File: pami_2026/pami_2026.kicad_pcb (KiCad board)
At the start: 4 copper layers, 50 x 50 mm, 71 parts, among them J1 Conn_01x02_Pin, J10 Conn_01x02_Pin, J2 Conn_01x03_Pin, J3 Conn_01x03_Pin, J4 Conn_01x03_Pin, J5 Conn_01x06, J6 Conn_01x06, J7 Conn_01x04_Pin, J8 Conn_01x04_Pin, J9 Conn_01x02_Pin, Q1 PMOS, Q2 PMOS, SW1 SW_Reed, U1 ESP32-WROOM-E, U2 AP63205WU, U3 DRV8871DDA, U5 AP63203WU, U6 DRV8871DDA

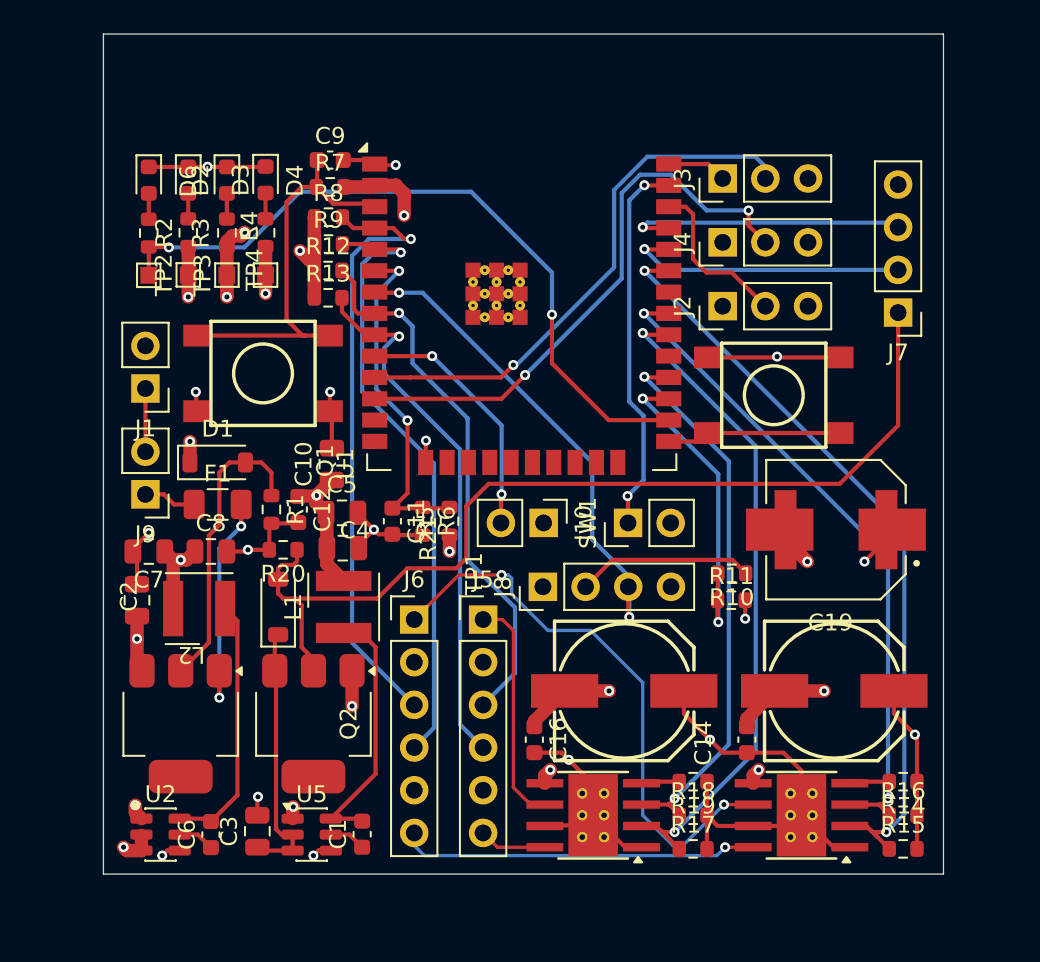
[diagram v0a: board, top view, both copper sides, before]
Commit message: FEAT : Via Stitching
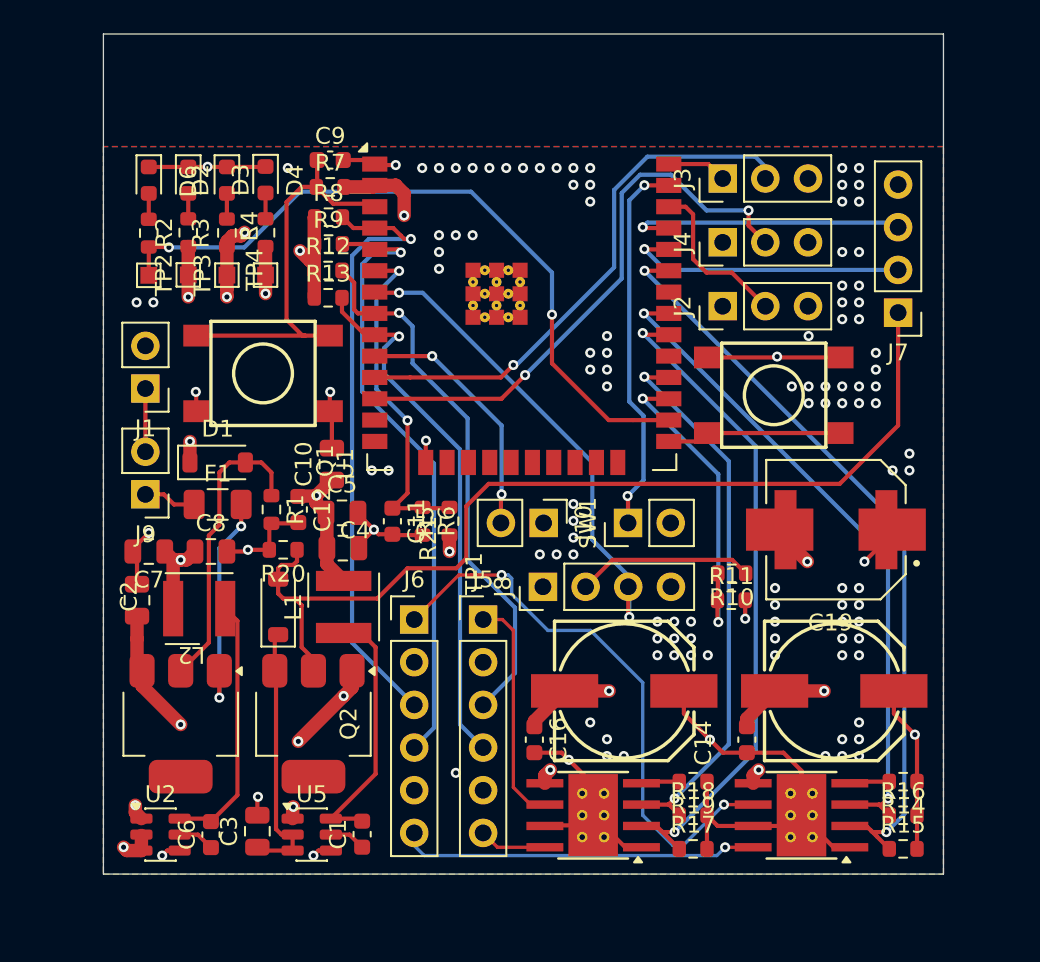
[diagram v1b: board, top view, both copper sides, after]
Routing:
- net BATT: track 28.1 -> 151.9 mm, vias 11 -> 12
- net +3.3V: track 80.5 -> 84.2 mm
- net GND: vias 17 -> 120
- added copper zone on B.Cu, net GND
- added copper zone on F.Cu, net GND
- added copper zone on In2.Cu, net GND
- removed copper zone on In2.Cu, net BATT

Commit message: Feat: mounting holes, indications, fix capa polarity
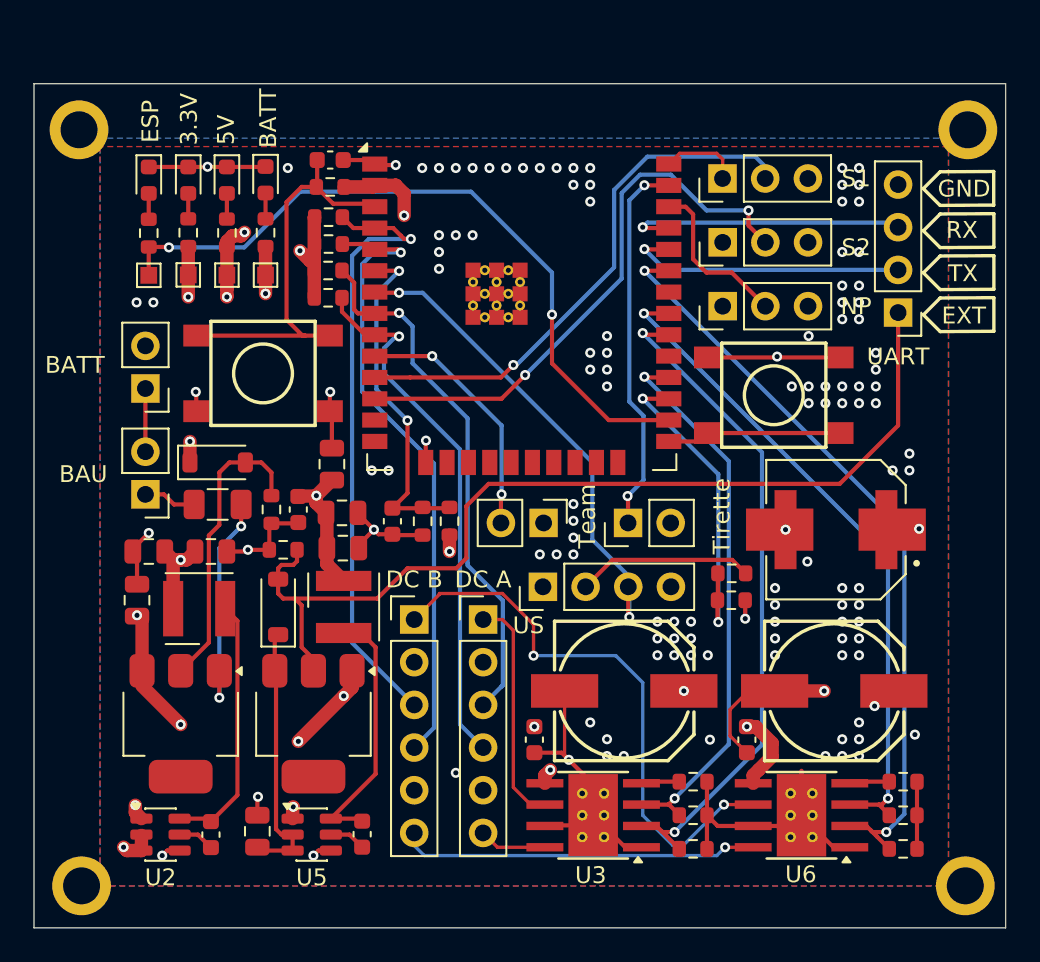
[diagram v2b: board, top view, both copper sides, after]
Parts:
- added H1: MountingHole, MountingHole:MountingHole_2.2mm_M2_ISO7380_Pad, F.Cu at (125.9, 124.0)
- added H2: MountingHole, MountingHole:MountingHole_2.2mm_M2_ISO7380_Pad, F.Cu at (178.5, 124.0)
- added H3: MountingHole, MountingHole:MountingHole_2.2mm_M2_ISO7380_Pad, F.Cu at (125.8, 79.0)
- added H4: MountingHole, MountingHole:MountingHole_2.2mm_M2_ISO7380_Pad, F.Cu at (178.7, 79.0)
- DC A: renamed from J5
- DC B: renamed from J6
- renumbered D2 to 3.3V, D3 to 5V, J1 to BATT, D4 to BATT, J9 to BAU, D6 to ESP, J2 to NP, J3 to S1, J4 to S2, J10 to Team, SW1 to Tirette, J7 to UART, J8 to US
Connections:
- C13 pad 1: GND -> BATT
- C13 pad 2: BATT -> GND
- C15 pad 1: GND -> BATT
- C15 pad 2: BATT -> GND
- C19 pad 1: GND -> BATT
- C19 pad 2: BATT -> GND
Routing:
- net BATT: track 151.9 -> 146.8 mm, vias 12 -> 14
- net GND: track 99.1 -> 96.1 mm, vias 120 -> 123
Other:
- board size 50 x 50 mm -> 57.8 x 50.2 mm
- board text added: "Cartes PAMIs 2026 V1"
- board text added: "EXT"
- board text added: "GND"
- board text added: "PIERSON Robin MARTINEZ Hugo"
- board text added: "RX"
- board text added: "TX"
- board text added: "U3"
- board text added: "U6"

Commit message: Feat: BOM LCSC + big plan de masse
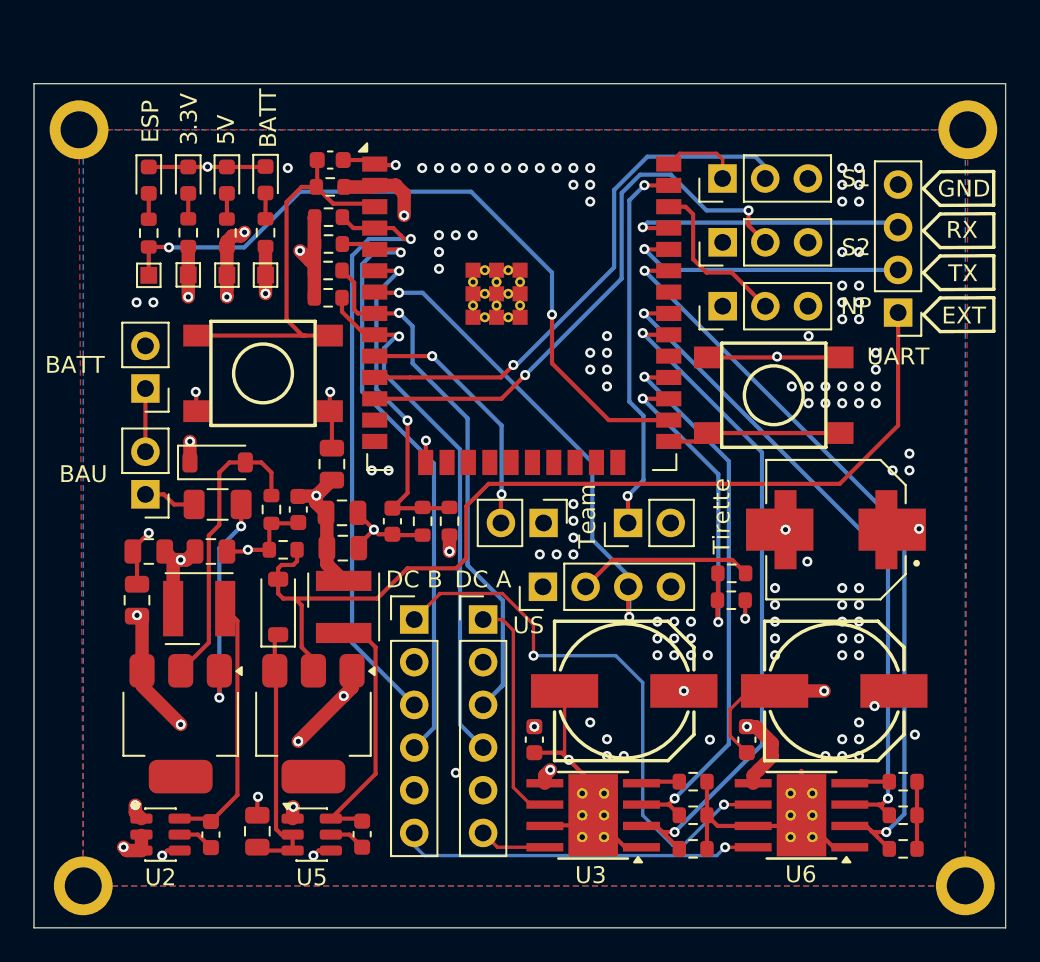
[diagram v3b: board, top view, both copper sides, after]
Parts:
- moved H1 0.10 mm to (126.0, 124.0)
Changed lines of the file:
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@@
 	(footprint "MountingHole:MountingHole_2.2mm_M2_ISO7380_Pad"
 		(layer "F.Cu")
-		(at 125.9 124)
+		(at 126 124)
 		(descr "Mounting Hole 2.2mm, M2, generated by kicad-footprint-generator mountinghole.py")
 		(tags "mountinghole M2 ISO7380")
@@
 		(polygon
 			(pts
-				(xy 177.5 80) (xy 127 80) (xy 127 124) (xy 177.5 124)
+				(xy 178.65 79) (xy 125.75 79) (xy 126 124) (xy 178.5 124)
 			)
 		)
@@
 		(polygon
 			(pts
-				(xy 177.5 79.5) (xy 127 79.5) (xy 127 124) (xy 177.5 124)
+				(xy 178.5 79) (xy 126 79) (xy 126 124) (xy 178.5 124)
+			)
+		)
+	)
+	(zone
+		(net 0)
+		(net_name "")
+		(layer "In1.Cu")
+		(hatch edge 0.5)
+		(connect_pads
+			(clearance 0)
+		)
+		(min_thickness 0.25)
+		(filled_areas_thickness no)
+		(keepout
+			(tracks not_allowed)
+			(vias not_allowed)
+			(pads not_allowed)
+			(copperpour not_allowed)
+			(footprints not_allowed)
+		)
+		(placement
+			(enabled no)
+			(sheetname "/")
+		)
+		(fill
+			(thermal_gap 0.5)
+			(thermal_bridge_width 0.5)
+		)
+		(polygon
+			(pts
+				(xy 176 58.5) (xy 128 58.5) (xy 128.113517 79.715135) (xy 176.622881 79.741622) (xy 176.5 58.5)
 			)
 		)
@@
 		(polygon
 			(pts
-				(xy 177.5 80) (xy 127 80) (xy 127 124) (xy 177.5 124)
+				(xy 178.5 79) (xy 126 79) (xy 126 124) (xy 178.5 124)
 			)
 		)
@@
 		(polygon
 			(pts
-				(xy 177.5 80) (xy 127 80) (xy 127 124) (xy 177.5 124)
+				(xy 178.5 79) (xy 126 79) (xy 126 124) (xy 178.5 124)
+			)
+		)
+	)
+	(zone
+		(net 0)
+		(net_name "")
+		(layer "In2.Cu")
+		(hatch edge 0.5)
+		(connect_pads
+			(clearance 0)
+		)
+		(min_thickness 0.25)
+		(filled_areas_thickness no)
+		(keepout
+			(tracks not_allowed)
+			(vias not_allowed)
+			(pads not_allowed)
+			(copperpour not_allowed)
+			(footprints not_allowed)
+		)
+		(placement
+			(enabled no)
+			(sheetname "/")
+		)
+		(fill
+			(thermal_gap 0.5)
+			(thermal_bridge_width 0.5)
+		)
+		(polygon
+			(pts
+				(xy 128 58.5) (xy 128.113977 79.715526) (xy 176.631036 79.717955) (xy 176.5 58.5)
 			)
 		)
